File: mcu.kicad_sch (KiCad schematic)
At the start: 19 parts, among them Q6 BC817W, Q7 BC817W, U4 ESP32-WROOM-32

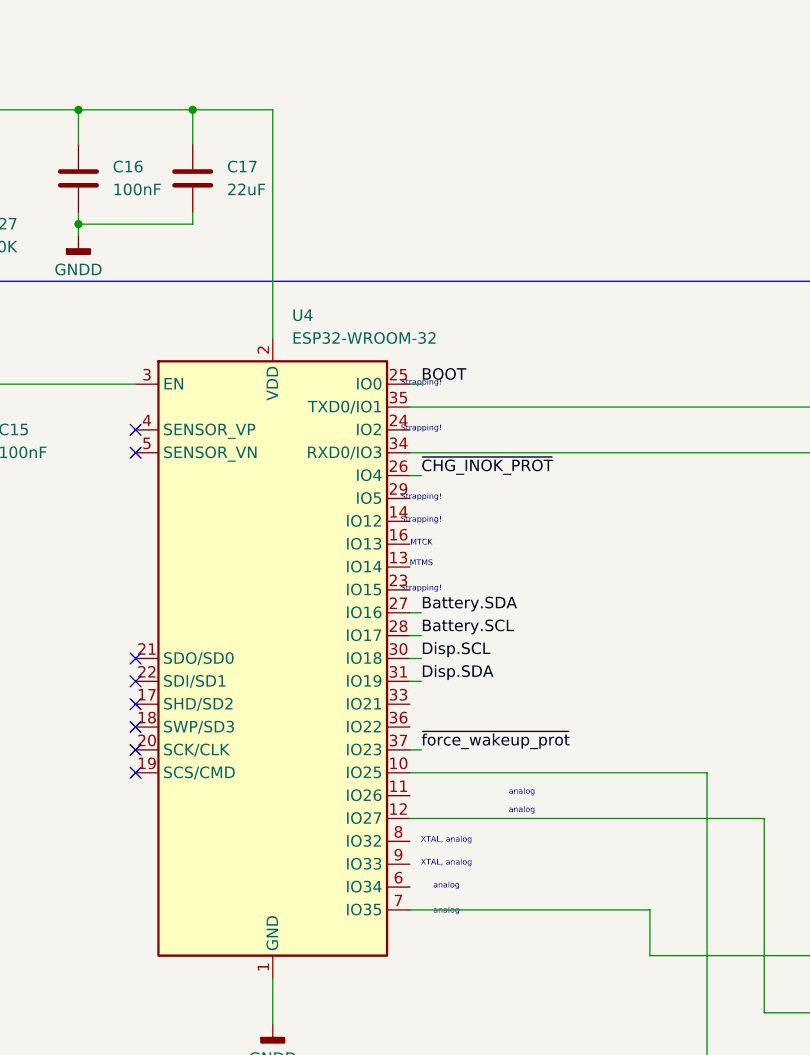
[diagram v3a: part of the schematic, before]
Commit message: Editing layout, redrawing analog and RTS DTS signals. Placing the silk layer designators
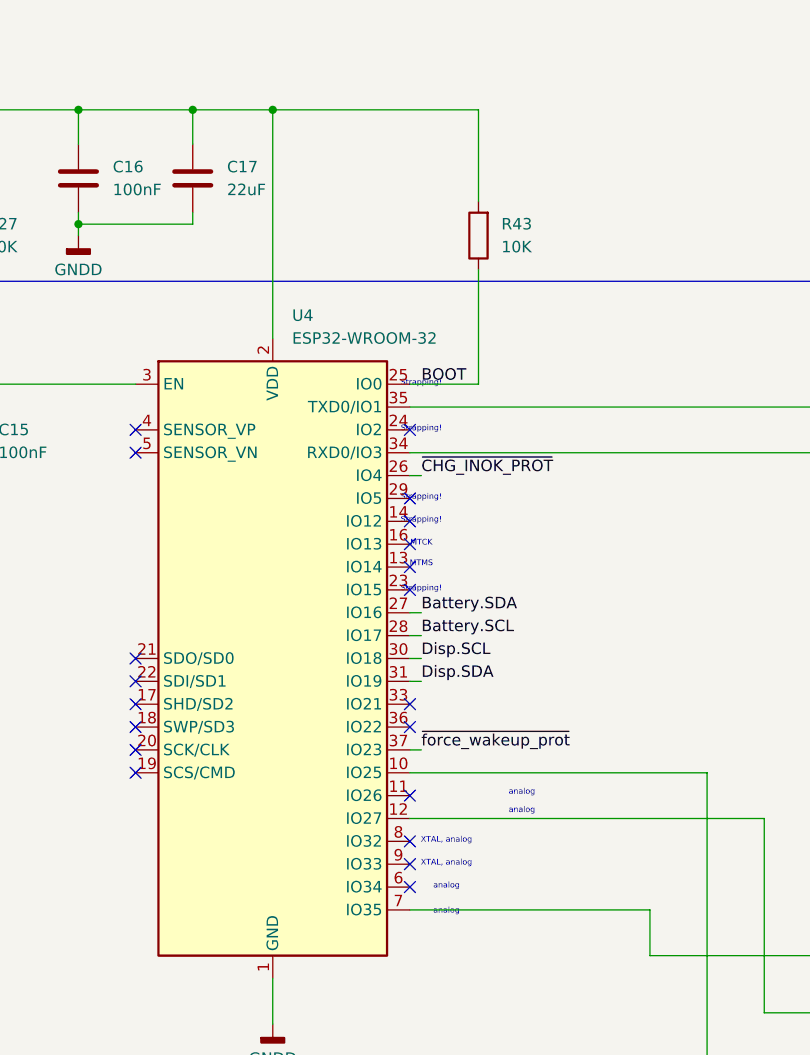
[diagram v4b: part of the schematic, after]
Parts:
- added R43: 10K, Resistor_SMD:R_0603_1608Metric_Pad0.98x0.95mm_HandSolder, symbol Device:R
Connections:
- net BOOT: now also R43.1
- net VDD: now also R43.2
- no-connect marks 8 -> 20
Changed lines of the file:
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@@
 	)
 	(junction
+		(at 123.19 25.4)
+		(diameter 0)
+		(color 0 0 0 0)
+	)
+	(junction
 		(at 114.3 25.4)
 		(diameter 0)
@@
 	)
 	(no_connect
+		(at 138.43 109.22)
+	)
+	(no_connect
+		(at 138.43 101.6)
+	)
+	(no_connect
+		(at 138.43 91.44)
+	)
+	(no_connect
+		(at 138.43 68.58)
+	)
+	(no_connect
+		(at 138.43 111.76)
+	)
+	(no_connect
 		(at 107.95 63.5)
 	)
 	(no_connect
+		(at 138.43 71.12)
+	)
+	(no_connect
+		(at 138.43 93.98)
+	)
+	(no_connect
 		(at 107.95 60.96)
 	)
 	(no_connect
+		(at 138.43 60.96)
+	)
+	(no_connect
+		(at 138.43 106.68)
+	)
+	(no_connect
 		(at 107.95 93.98)
 	)
 	(no_connect
+		(at 138.43 73.66)
+	)
+	(no_connect
 		(at 107.95 86.36)
 	)
@@
 		(at 107.95 96.52)
 	)
+	(no_connect
+		(at 138.43 78.74)
+	)
+	(no_connect
+		(at 138.43 76.2)
+	)
 	(bus_entry
 		(at 236.22 91.44)
@@
 	(wire
 		(pts
+			(xy 146.05 35.56) (xy 146.05 25.4)
+		)
+		(stroke
+			(width 0)
+			(type default)
+		)
+	)
+	(wire
+		(pts
 			(xy 38.1 31.75) (xy 38.1 38.1)
 		)
@@
 	(wire
 		(pts
+			(xy 146.05 25.4) (xy 123.19 25.4)
+		)
+		(stroke
+			(width 0)
+			(type default)
+		)
+	)
+	(wire
+		(pts
 			(xy 138.43 104.14) (xy 177.8 104.14)
 		)
@@
 	(wire
 		(pts
-			(xy 138.43 55.88) (xy 139.7 55.88)
+			(xy 138.43 55.88) (xy 146.05 55.88)
 		)
 		(stroke
@@
 	(wire
 		(pts
+			(xy 146.05 43.18) (xy 146.05 55.88)
+		)
+		(stroke
+			(width 0)
+			(type default)
+		)
+	)
+	(wire
+		(pts
 			(xy 123.19 121.92) (xy 123.19 127)
 		)
@@
 					(unit 1)
 				)
+			)
+		)
+	)
+	(symbol
+		(lib_id "Device:R")
+		(at 146.05 39.37 180)
+		(unit 1)
+		(body_style 1)
+		(exclude_from_sim no)
+		(in_bom yes)
+		(on_board yes)
+		(in_pos_files yes)
+		(dnp no)
+		(fields_autoplaced yes)
+		(property "Reference" "R43"
+			(at 148.59 38.0999 0)
+			(show_name no)
+			(do_not_autoplace no)
+			(effects
+				(font
+					(size 1.27 1.27)
+				)
+				(justify right)
+			)
+		)
+		(property "Value" "10K"
+			(at 148.59 40.6399 0)
+			(show_name no)
+			(do_not_autoplace no)
+			(effects
+				(font
+					(size 1.27 1.27)
+				)
+				(justify right)
+			)
+		)
+		(property "Footprint" "Resistor_SMD:R_0603_1608Metric_Pad0.98x0.95mm_HandSolder"
+			(at 147.828 39.37 90)
+			(hide yes)
+			(show_name no)
+			(do_not_autoplace no)
+			(effects
+				(font
+					(size 1.27 1.27)
+				)
+			)
+		)
+		(property "Datasheet" ""
+			(at 146.05 39.37 0)
+			(hide yes)
+			(show_name no)
+			(do_not_autoplace no)
+			(effects
+				(font
+					(size 1.27 1.27)
+				)
+			)
+		)
+		(property "Description" "Resistor"
+			(at 146.05 39.37 0)
+			(hide yes)
+			(show_name no)
+			(do_not_autoplace no)
+			(effects
+				(font
+					(size 1.27 1.27)
+				)
+			)
+		)
+		(pin "1"
+		)
+		(pin "2"
+		)
+		(instances
+			(project "MoistureESP"
+				(path "/f2b9f638-139e-46ec-aa60-77c4af989196/0ddaa739-ba4f-4157-bc77-184906368825"
+					(reference "R43")
+					(unit 1)
+				)

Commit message: Export BOM, change page headers.
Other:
- company: (none) -> B.Major
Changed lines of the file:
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@@
 	(generator_version "10.0")
 	(paper "A4")
+	(title_block
+		(date "2026-03-27")
+		(rev "1")
+		(company "B.Major")
+	)
 	(text "analog"
 		(exclude_from_sim no)
